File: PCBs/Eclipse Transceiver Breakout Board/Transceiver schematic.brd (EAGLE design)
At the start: 25.4 x 30.2 mm, 3 parts, among them J1 2X6 FEMALE, U1 RFM95W-868S2

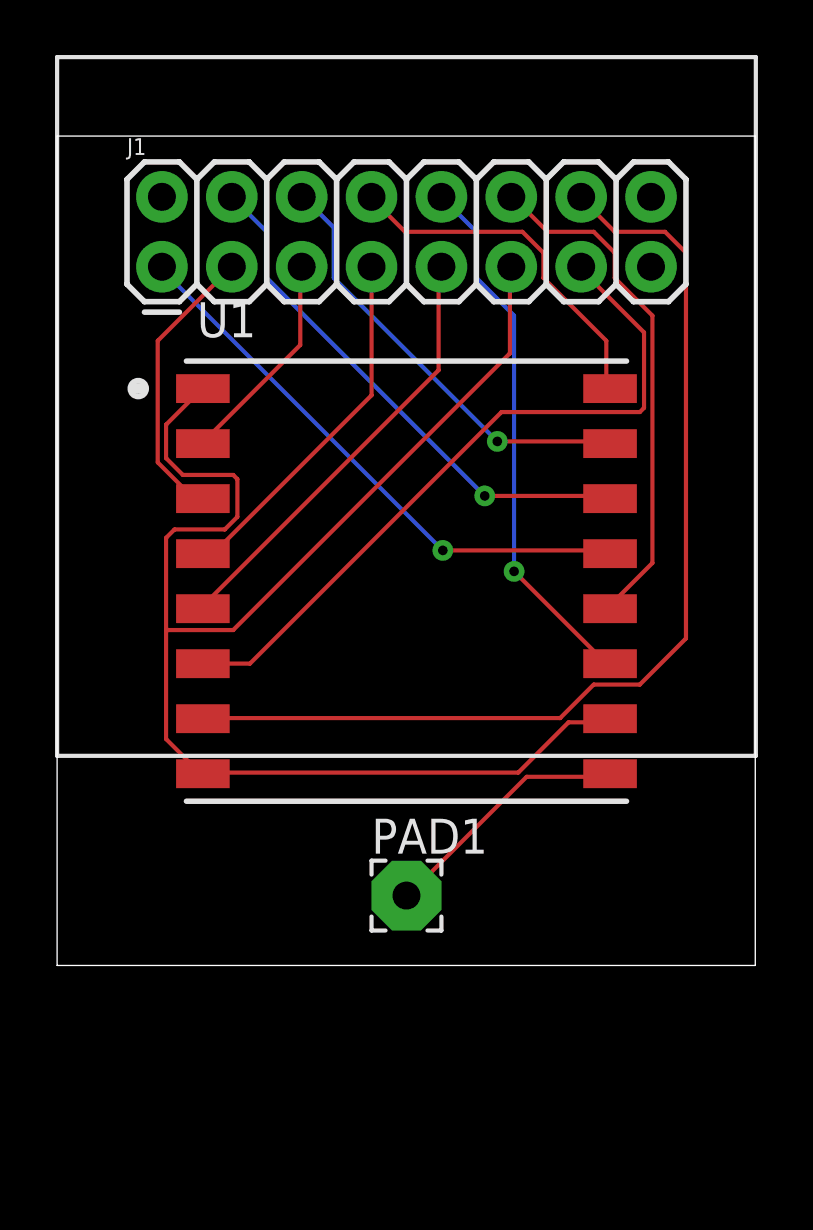
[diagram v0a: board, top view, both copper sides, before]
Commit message: Final Update
This is the design for the board that was milled and used for the RTR testing.
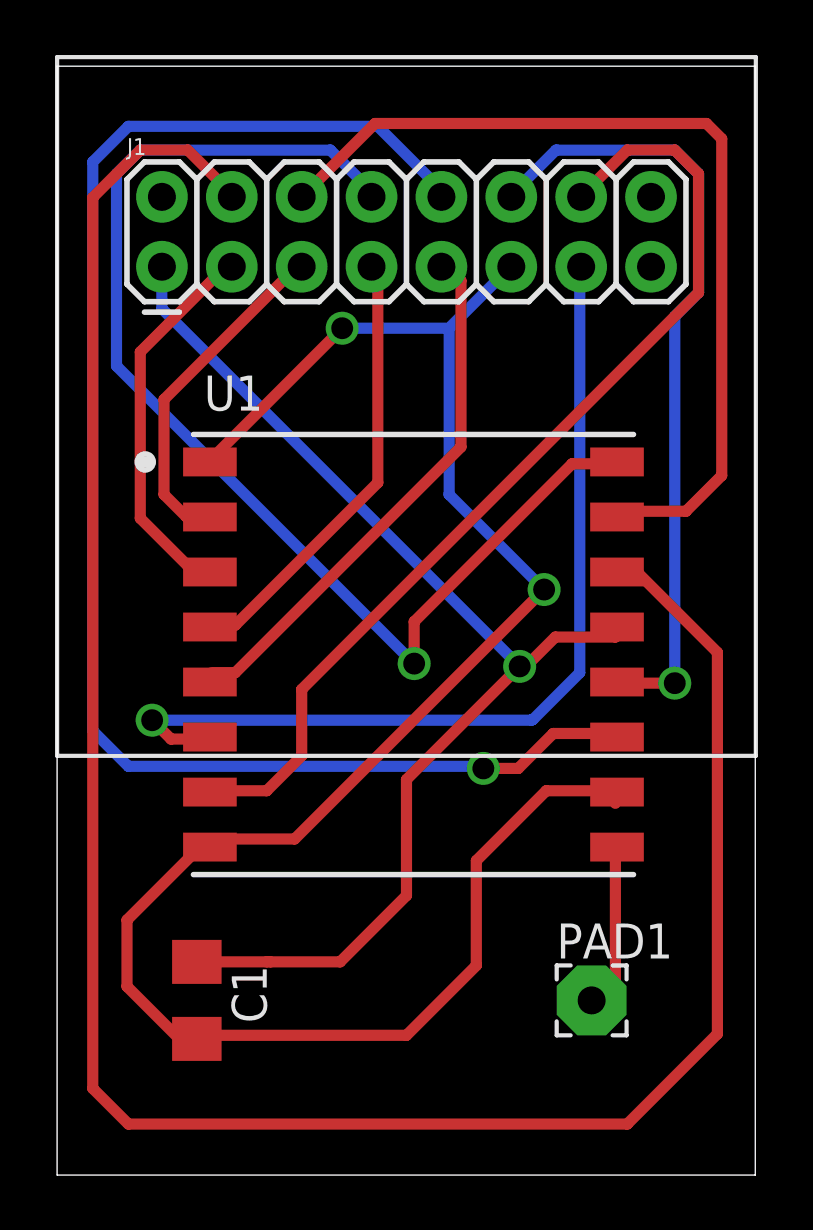
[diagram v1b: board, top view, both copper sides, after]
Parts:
- added C1: .1uF, RTR:C1206
- moved PAD1 7.73 mm to (19.4, -8.89)
- moved U1 2.68 mm to (13.0, 3.68)
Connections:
- net N$10 renamed SPI1_GPIO3
- net N$11 renamed SPI1_GPIO4
- net N$13 renamed RESET
- net N$14 renamed SPI1_GPIO5
- net N$3 renamed SPI1_MISO
- net N$4 renamed SPI1_CLK
- net N$6 renamed SPI1_GPIO0
- net N$7 renamed SPI1_CS
- net N$8 renamed SPI1_GPIO1
- net N$9 renamed SPI1_GPIO2
- removed net N$1: J1.11, U1.1, U1.10, U1.8
- removed net N$2: J1.3, U1.3
- removed net N$5: J1.1, U1.13
- new net GND: C1.2, J1.11, U1.1, U1.10, U1.8
- new net SPI1_MOSI: J1.3
- new net VCC: C1.1, J1.1, U1.13
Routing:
- net GND: track 0.00 -> 73.3 mm, vias 0 -> 2
- net SPI1_GPIO0: track 19.3 -> 81.8 mm, vias 1 -> 0
- net N$1: track 54.9 -> 0.00 mm
- net VCC: track 0.00 -> 43.3 mm, vias 0 -> 1
- net SPI1_GPIO3: track 19.6 -> 55.1 mm
- net SPI1_GPIO2: track 13.1 -> 43.9 mm, vias 0 -> 1
- net N$5: track 20.7 -> 0.00 mm, vias 1 -> 0
- net SPI1_GPIO1: track 16.0 -> 33.0 mm, vias 1 -> 0
- net SPI1_MOSI: track 0.00 -> 13.5 mm
- net N$2: track 10.4 -> 0.00 mm
- net SPI1_GPIO4: track 18.7 -> 28.8 mm, vias 0 -> 1
- net RESET: track 26.0 -> 32.9 mm, vias 0 -> 1
- net SPI1_MISO: track 7.90 -> 12.4 mm
- net SPI1_CS: track 16.0 -> 19.4 mm
- net N$12: track 9.22 -> 6.02 mm
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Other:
- board size 25.4 x 30.2 mm -> 25.4 x 40.3 mm
